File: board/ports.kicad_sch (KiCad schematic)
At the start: 2 parts, among them U15 PORTS

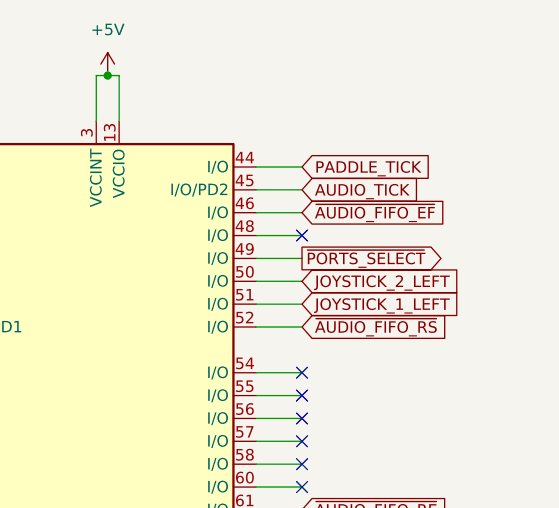
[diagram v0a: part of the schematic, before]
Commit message: add AUDIO_FIFO sheet; fix PORTS ~AUDIO_FIFO_EF onto pin 48
Co-Authored-By: Claude Fable 5.1 <noreply@anthropic.com>
Claude-Session: https://claude.ai/code/session_01NsFH8WNb3Tja14xUfwuyqj
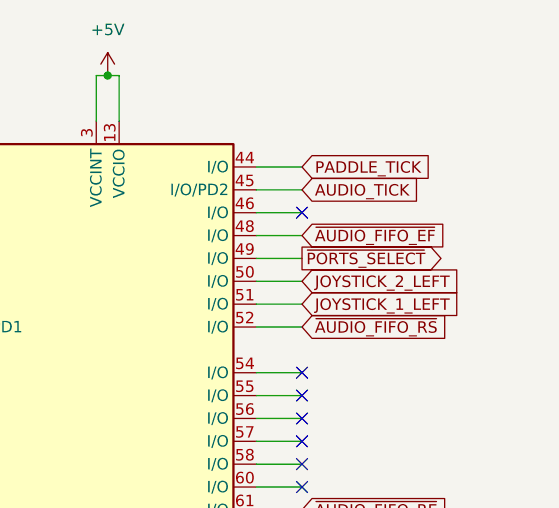
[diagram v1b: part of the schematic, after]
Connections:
- net ~{AUDIO_FIFO_EF}: now also U15.48 (I/O); no longer U15.46 (I/O)
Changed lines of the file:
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@@
 	)
 	(no_connect
-		(at 118.11 82.55)
+		(at 118.11 80.01)
 	)
 	(no_connect
@@
 	(global_label "~{AUDIO_FIFO_EF}"
 		(shape input)
-		(at 118.11 80.01 0)
+		(at 118.11 82.55 0)
 		(fields_autoplaced yes)
 		(effects
@@
 		)
 		(property "Intersheetrefs" "${INTERSHEET_REFS}"
-			(at 135.0049 80.01 0)
-			(effects
-				(font
+			(at 135.0049 82.55 0)
+			(effects
+				(font
